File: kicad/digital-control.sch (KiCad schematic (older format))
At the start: 29 parts, among them J3 CONN_01X04, Q3 MMBT3904, SW1 JS5208, U4 STM32F031G, U5 SSD1306-OLED-I2C, U6 MMA8652FC

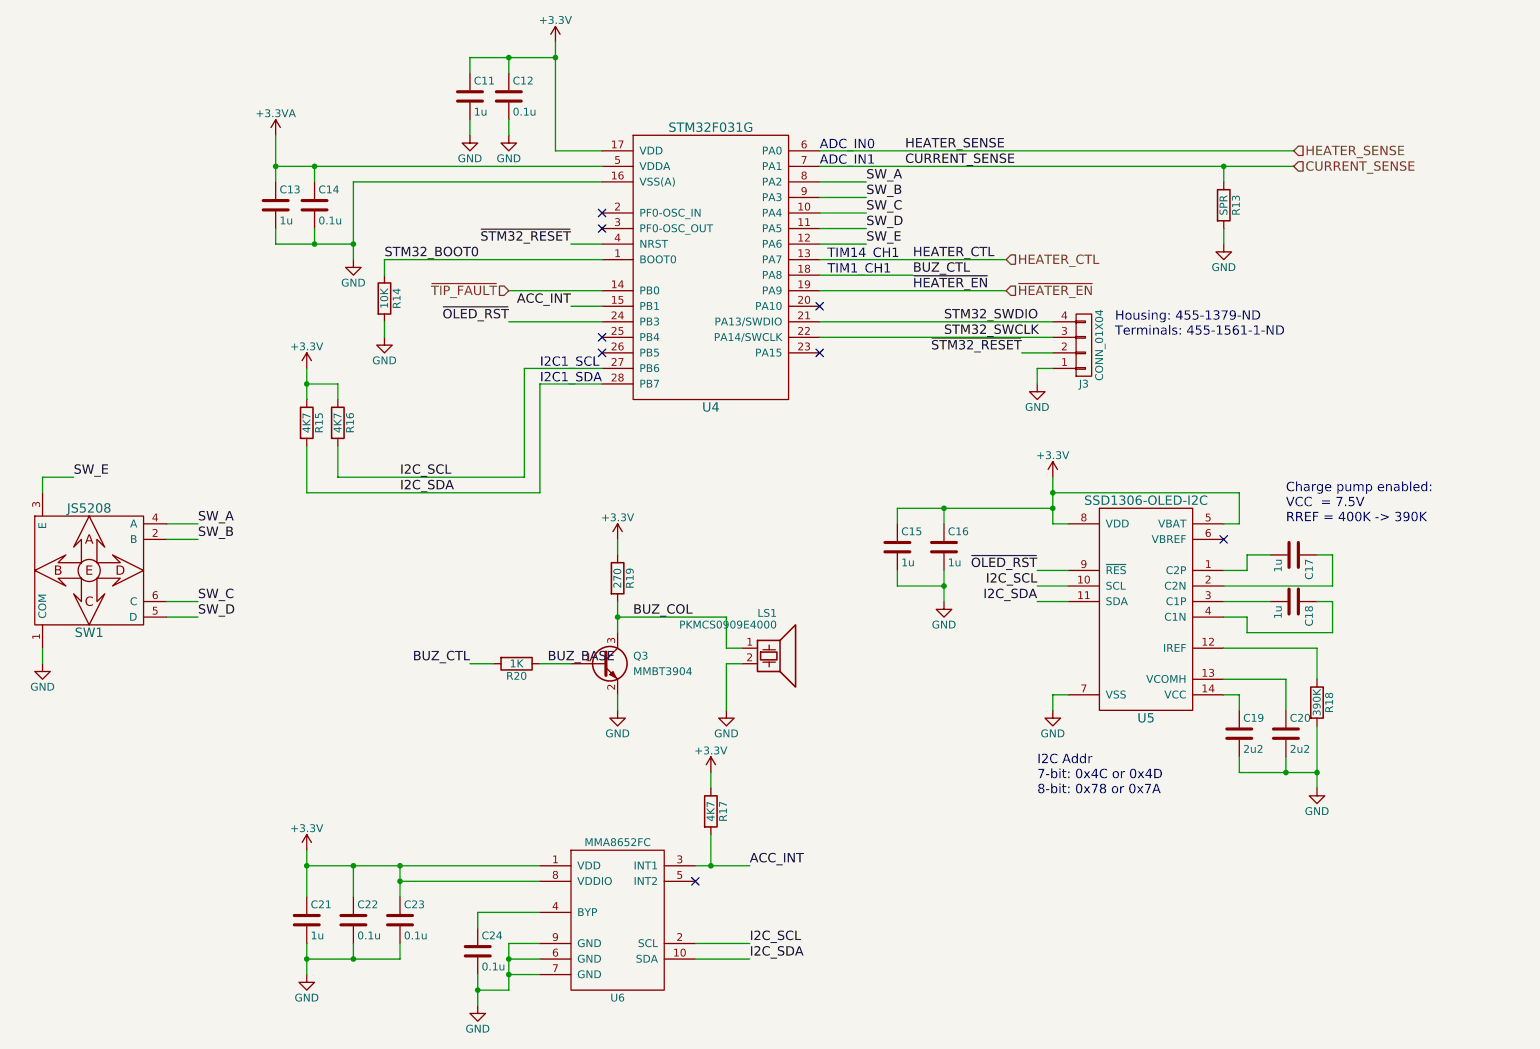
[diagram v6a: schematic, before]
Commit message: Fixed thermal cutoff circuit and finished footprint selection
The main issue with the thermal cutoff was the open-collector maximum
voltage. I had to find a (slightly more expensive) comparator with an
output that was tolerant. Other comparators that would be instead
tolerant of being run off 12V were about the same price.

The fuse I'm not sure about. I'm just going to short it out. The
regulator can handle a short circuit and so can the crowbar. I also
couldn't decide where to put the feedback network. If I put it after the
fuse it would compensate for any voltage drop across it. However, it
would also cause the regulator to try to boost the voltage insanely high
during a short circuit across the fuse and maybe cause it to pop (I
could really only find ones rated to 6V). I instead placed it before the
fuse. I'm still not sure.
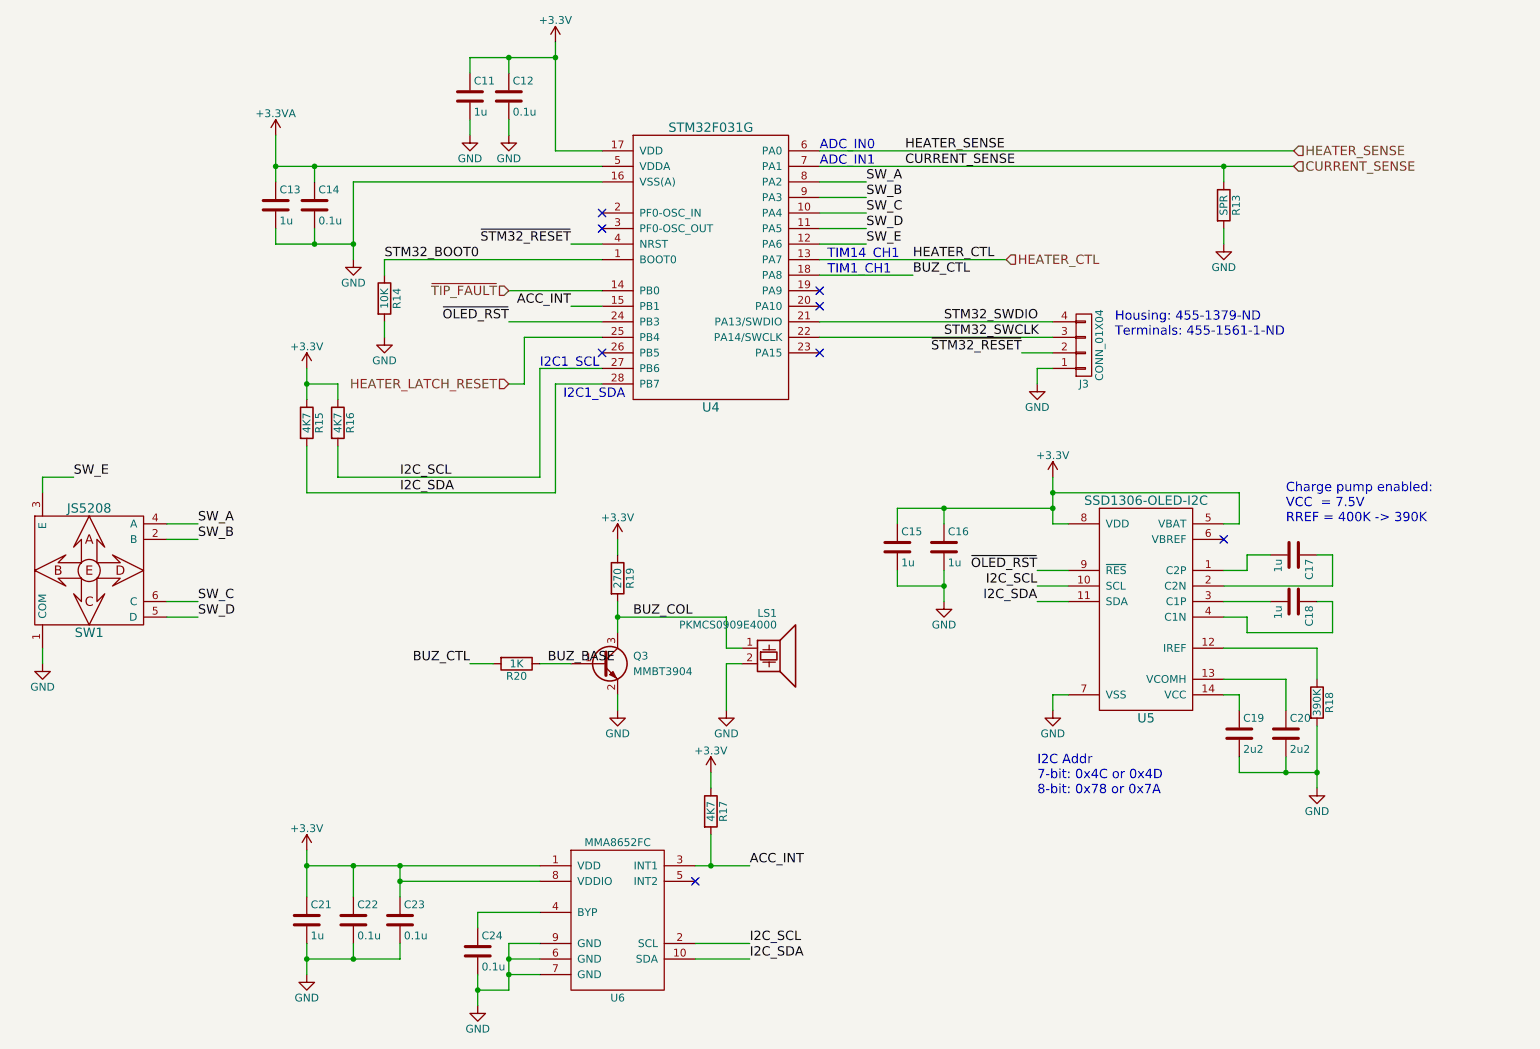
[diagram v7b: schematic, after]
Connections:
- net HEATER_LATCH_RESET: now reaches U4.25 (PB4)
- net ~HEATER_EN: no longer names the net of U4.19 (PA9)
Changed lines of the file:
@@
 $EndDescr
-$Comp
-L STM32F031G U4
-U 1 1 59208351
-P 5600 2450
-F 0 "U4" H 5600 1550 60  0000 C CNN
-F 1 "STM32F031G" H 5600 3350 60  0000 C CNN
-F 2 "rt-soldering-iron:28-UFQFPN" H 5400 2300 60  0001 C CNN
-F 3 "" H 5400 2300 60  0001 C CNN
-F 4 "497-13619-ND" H 5600 2450 60  0001 C CNN "Part No."
-	1    5600 2450
-	1    0    0    -1
-$EndComp
 $Comp
 L +3.3V #PWR042
@@
 	4600 1700 4900 1700
 Wire Wire Line
-	4600 1000 4600 1700
+	4600 1000 4600 1100
+Wire Wire Line
+	4600 1100 4600 1700
 $Comp
 L C C14
@@
 $EndComp
 Wire Wire Line
-	3300 1900 3300 2400
+	3300 1900 3300 2300
+Wire Wire Line
+	3300 2300 3300 2400
 Wire Wire Line
 	3300 1900 4900 1900
@@
 Connection ~ 3050 1800
 Wire Wire Line
-	2800 2300 3300 2300
+	2800 2300 3050 2300
+Wire Wire Line
+	3050 2300 3300 2300
 Wire Wire Line
 	3050 2300 3050 2200
@@
 	4300 1200 4300 1100
 Wire Wire Line
-	4050 1100 4600 1100
+	4050 1100 4300 1100
+Wire Wire Line
+	4300 1100 4600 1100
 Connection ~ 4600 1100
 $Comp
@@
 $EndComp
 Wire Wire Line
-	2800 1600 2800 1900
+	2800 1600 2800 1800
+Wire Wire Line
+	2800 1800 2800 1900
 Connection ~ 2800 1800
 Wire Wire Line
@@
 	3500 2900 3500 2800
 Wire Wire Line
-	2800 1800 4900 1800
+	2800 1800 3050 1800
+Wire Wire Line
+	3050 1800 4900 1800
 $Comp
 L +3.3VA #PWR047
@@
 $EndComp
 Wire Wire Line
-	4900 3100 4400 3100
-Wire Wire Line
-	4400 3100 4400 3800
-Wire Wire Line
-	4400 3800 3200 3800
+	4900 3100 4500 3100
+Wire Wire Line
+	4500 3100 4500 3800
+Wire Wire Line
+	4500 3800 3200 3800
 Wire Wire Line
 	3200 3800 3200 3600
 Wire Wire Line
-	4900 3200 4500 3200
-Wire Wire Line
-	4500 3200 4500 3900
-Wire Wire Line
-	4500 3900 3000 3900
+	4900 3200 4600 3200
+Wire Wire Line
+	4600 3200 4600 3900
+Wire Wire Line
+	4600 3900 3000 3900
 Wire Wire Line
 	3000 3900 3000 3600
@@
 $EndComp
 Wire Wire Line
-	3000 3100 3000 3300
+	3000 3100 3000 3200
+Wire Wire Line
+	3000 3200 3000 3300
 Wire Wire Line
 	3000 3200 3200 3200
@@
 $EndComp
 Wire Wire Line
-	7800 3800 7800 4100
+	7800 3800 7800 3900
+Wire Wire Line
+	7800 3900 7800 4000
+Wire Wire Line
+	7800 4000 7800 4100
 Wire Wire Line
 	7800 4100 7900 4100
@@
 $EndComp
 Wire Wire Line
-	3000 6300 4500 6300
-Wire Wire Line
-	3600 6300 3600 6500
+	3000 6300 3300 6300
+Wire Wire Line
+	3300 6300 3600 6300
+Wire Wire Line
+	3600 6300 4500 6300
+Wire Wire Line
+	3600 6300 3600 6400
+Wire Wire Line
+	3600 6400 3600 6500
 Wire Wire Line
 	4500 6400 3600 6400
@@
 Connection ~ 3600 6300
 Wire Wire Line
-	3000 6200 3000 6500
+	3000 6200 3000 6300
+Wire Wire Line
+	3000 6300 3000 6500
 Connection ~ 3300 6300
 $Comp
@@
 Connection ~ 3000 6300
 Wire Wire Line
-	3000 6800 3000 7000
-Wire Wire Line
-	3000 6900 3600 6900
+	3000 6800 3000 6900
+Wire Wire Line
+	3000 6900 3000 7000
+Wire Wire Line
+	3000 6900 3300 6900
+Wire Wire Line
+	3300 6900 3600 6900
 Wire Wire Line
 	3600 6900 3600 6800
@@
 $EndComp
 Wire Wire Line
-	4100 7000 4100 7200
+	4100 7000 4100 7100
+Wire Wire Line
+	4100 7100 4100 7200
 Wire Wire Line
 	4300 7100 4100 7100
 Wire Wire Line
-	4300 6800 4300 7100
+	4300 6800 4300 6900
+Wire Wire Line
+	4300 6900 4300 7000
+Wire Wire Line
+	4300 7000 4300 7100
 Wire Wire Line
 	4300 6800 4500 6800
@@
 Text Notes 4500 3100 0    60   ~ 0
 I2C1_SCL
-Text Notes 4500 3200 0    60   ~ 0
+Text Notes 4650 3300 0    60   ~ 0
 I2C1_SDA
 Text Notes 9300 4100 0    60   ~ 0
@@
 $EndComp
 Wire Wire Line
-	9500 5400 9500 5800
+	9500 5400 9500 5700
+Wire Wire Line
+	9500 5700 9500 5800
 $Comp
 L C C15
@@
 $EndComp
 Wire Wire Line
-	6800 4000 7800 4000
+	6800 4000 7100 4000
+Wire Wire Line
+	7100 4000 7800 4000
 Wire Wire Line
 	6800 4000 6800 4100
@@
 $EndComp
 Wire Wire Line
-	7100 4400 7100 4600
+	7100 4400 7100 4500
+Wire Wire Line
+	7100 4500 7100 4600
 Wire Wire Line
 	7100 4500 6800 4500
@@
 ACC_INT
 Wire Wire Line
-	5500 6300 5850 6300
+	5500 6300 5600 6300
+Wire Wire Line
+	5600 6300 5850 6300
 NoConn ~ 5500 6400
 Text HLabel 9350 1800 2    60   Input ~ 0
 CURRENT_SENSE
 Wire Wire Line
-	6300 1800 9350 1800
+	6300 1800 8900 1800
+Wire Wire Line
+	8900 1800 9350 1800
 Text Notes 6300 1800 0    60   ~ 0
 ADC_IN1
@@
 $EndComp
 Wire Wire Line
-	9000 5700 9500 5700
+	9000 5700 9300 5700
+Wire Wire Line
+	9300 5700 9500 5700
 Wire Wire Line
 	9000 5700 9000 5600
@@
 Wire Wire Line
 	5600 5700 5600 5800
-NoConn ~ 4900 2900
 NoConn ~ 4900 3000
 NoConn ~ 6300 2700
@@
 	5000 5200 5000 5300
 Wire Wire Line
-	5000 4800 5000 4600
+	5000 4800 5000 4700
+Wire Wire Line
+	5000 4700 5000 4600
 Wire Wire Line
 	5000 4700 5700 4700
@@
 Text Label 5100 4700 0    60   ~ 0
 BUZ_COL
-Text HLabel 7500 2600 2    60   Input ~ 0
-~HEATER_EN
-Wire Wire Line
-	7500 2600 6300 2600
-Text Label 6900 2600 0    60   ~ 0
-~HEATER_EN
+Text HLabel 4300 3200 0    60   Input ~ 0
+HEATER_LATCH_RESET
+$Comp
+L STM32F031G U4
+U 1 1 59208351
+P 5600 2450
+F 0 "U4" H 5600 1550 60  0000 C CNN
+F 1 "STM32F031G" H 5600 3350 60  0000 C CNN
+F 2 "rt-soldering-iron:28-UFQFPN" H 5400 2300 60  0001 C CNN
+F 3 "" H 5400 2300 60  0001 C CNN
+F 4 "497-13619-ND" H 5600 2450 60  0001 C CNN "Part No."
+	1    5600 2450
+	1    0    0    -1
+$EndComp
+Wire Wire Line
+	4900 2900 4400 2900
+Wire Wire Line
+	4400 2900 4400 3200
+Wire Wire Line
+	4400 3200 4300 3200
+NoConn ~ 6300 2600
 $EndSCHEMATC

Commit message: Changed out switch for two small side clicker ones
Should make things a little easier to lay out and easier to modify
later.
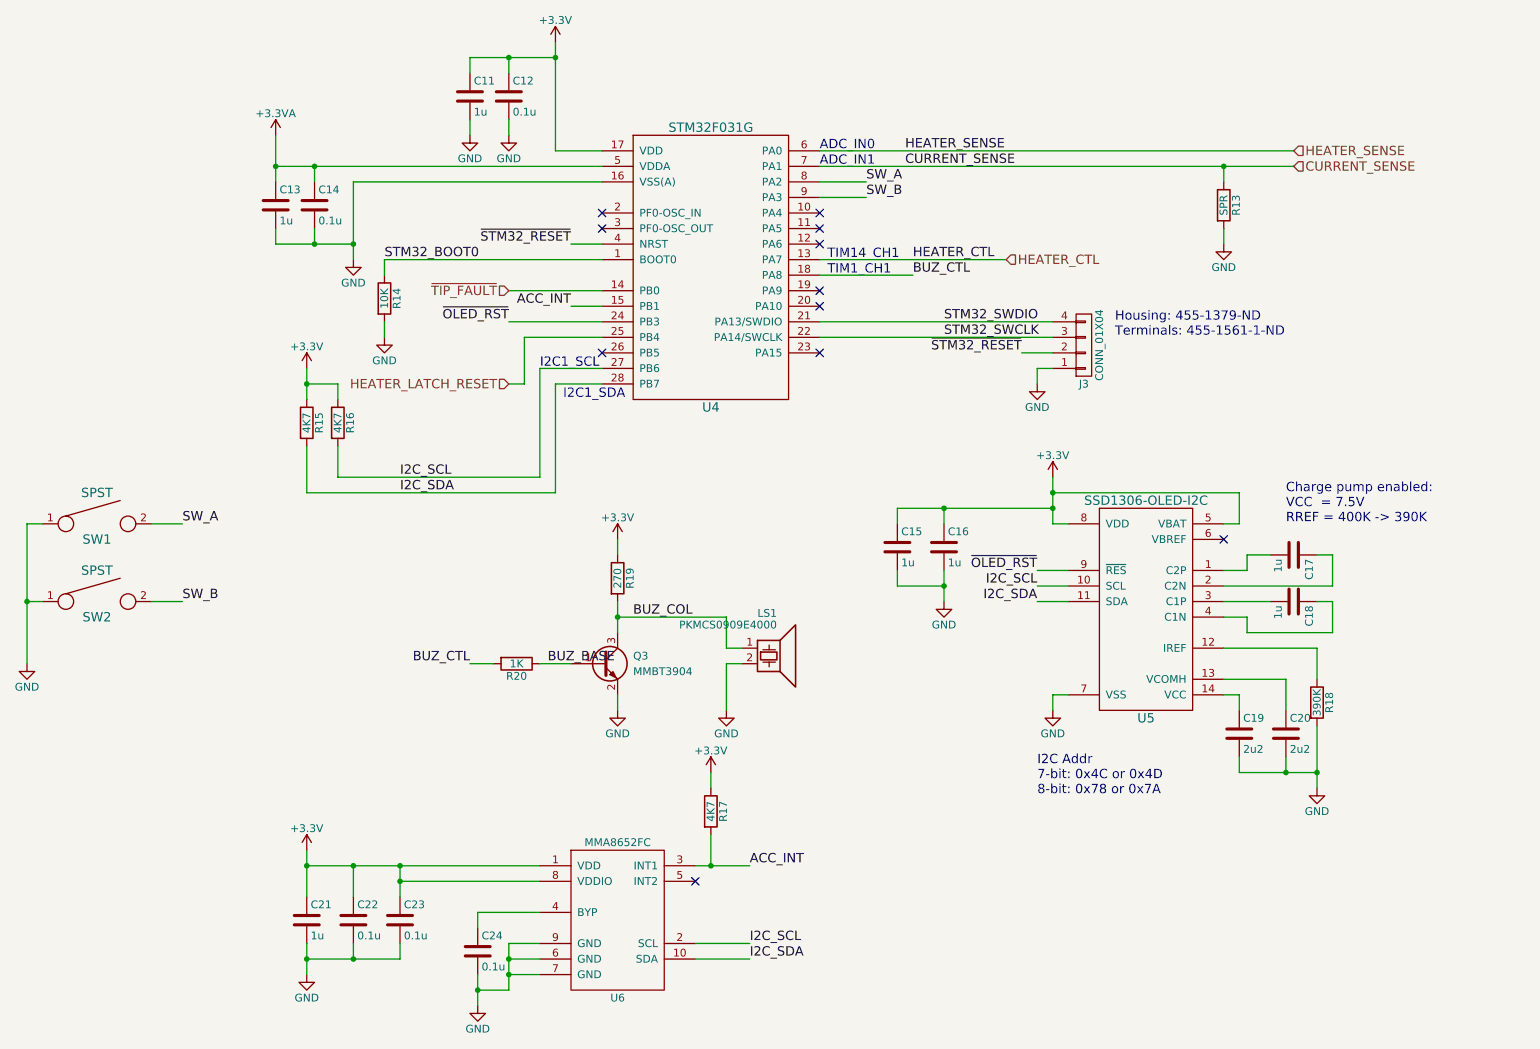
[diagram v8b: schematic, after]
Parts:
- removed SW1: JS5208, rt-soldering-iron:JS5208, symbol JS5208
- added SW1, SW2: SPST, rt-soldering-iron:Panasonic_EVQP4, symbol SPST
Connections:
- net GND: now also SW1.1, SW2.1
- net SW_A: now also SW1.2
- net SW_B: now also SW2.2
- net SW_C: no longer names the net of U4.10 (PA4)
- net SW_D: no longer names the net of U4.11 (PA5)
- net SW_E: no longer names the net of U4.12 (PA6)
- no-connect marks 8 -> 11
